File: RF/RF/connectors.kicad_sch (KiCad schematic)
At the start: 0 parts

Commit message: added external memory
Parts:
- added J601: Conn_01x02, Connector_PinHeader_2.00mm:PinHeader_1x02_P2.00mm_Vertical, symbol Connector_Generic:Conn_01x02
- added J602: Conn_01x06, Connector_PinHeader_2.00mm:PinHeader_1x06_P2.00mm_Vertical, symbol Connector_Generic:Conn_01x06
- added J603: Conn_02x05_Odd_Even, Connector_PinHeader_1.27mm:PinHeader_2x04_P1.27mm_Vertical_SMD, symbol Connector_Generic:Conn_02x05_Odd_Even
- added R601: DNP, Resistor_SMD:R_4020_10251Metric_Pad1.65x5.30mm_HandSolder, symbol Device:R
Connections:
- new net: J602.3 (Pin_3), R601.1
- new net +3.3V: J601.1 (Pin_1), J603.2 (Pin_2), R601.2
- new net +3.3VADC: J603.9 (Pin_9)
- new net CC_DC: J603.3 (Pin_3)
- new net CC_DD: J603.4 (Pin_4)
- new net CC_SPI_MISO: J603.10 (Pin_10)
- new net CC_SPI_MOSI: J603.8 (Pin_8)
- new net CC_SPI_SCK: J603.6 (Pin_6)
- new net GND: J601.2 (Pin_2), J602.1 (Pin_1), J603.1 (Pin_1)
- new net UART0_CTS: J602.6 (Pin_6)
- new net UART0_RTS: J602.2 (Pin_2)
- new net UART0_RX: J602.4 (Pin_4)
- new net UART0_TX: J602.5 (Pin_5)
- new net ~{CC_SPI_SSN}: J603.5 (Pin_5)
- new net ~{RESET}: J603.7 (Pin_7)
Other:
- note added: "(3V3 from debugger)"
- note added: "CC DEBUGGER"
- note added: "POWER INPUT"
- note added: "UART HEADER"

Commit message: RF: Push for schematic capture review version 1.0
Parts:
- J601: footprint Connector_PinHeader_2.00mm:PinHeader_1x02_P2.00mm_Vertical -> Connector_PinHeader_1.27mm:PinHeader_1x02_P1.27mm_Vertical
- J602: footprint Connector_PinHeader_2.00mm:PinHeader_1x06_P2.00mm_Vertical -> Connector_PinHeader_1.27mm:PinHeader_1x06_P1.27mm_Vertical
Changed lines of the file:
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@@
   )
   (rectangle (start 166.624 75.692) (end 229.362 104.648)
-    (stroke (width 0) (type default))
+    (stroke (width 0.5) (type default))
     (fill (type none))
   )
   (rectangle (start 52.324 73.66) (end 99.314 101.6)
-    (stroke (width 0) (type default))
+    (stroke (width 0.5) (type default))
     (fill (type none))
   )
   (rectangle (start 113.03 75.692) (end 148.59 99.06)
-    (stroke (width 0) (type default))
+    (stroke (width 0.5) (type default))
     (fill (type none))
   )
@@
       (effects (font (size 1.27 1.27)) (justify left))
     )
-    (property "Footprint" "Connector_PinHeader_2.00mm:PinHeader_1x02_P2.00mm_Vertical" (at 127.762 87.63 0)
+    (property "Footprint" "Connector_PinHeader_1.27mm:PinHeader_1x02_P1.27mm_Vertical" (at 127.762 87.63 0)
       (effects (font (size 1.27 1.27)) hide)
     )
@@
       (effects (font (size 1.27 1.27)) (justify left))
     )
-    (property "Footprint" "Connector_PinHeader_2.00mm:PinHeader_1x06_P2.00mm_Vertical" (at 67.31 90.678 0)
-      (effects (font (size 1.27 1.27)) hide)
-    )
+    (property "Footprint" "Connector_PinHeader_1.27mm:PinHeader_1x06_P1.27mm_Vertical" (at 67.31 90.678 0)
+      (effects (font (size 1.27 1.27)) hide)
+    )

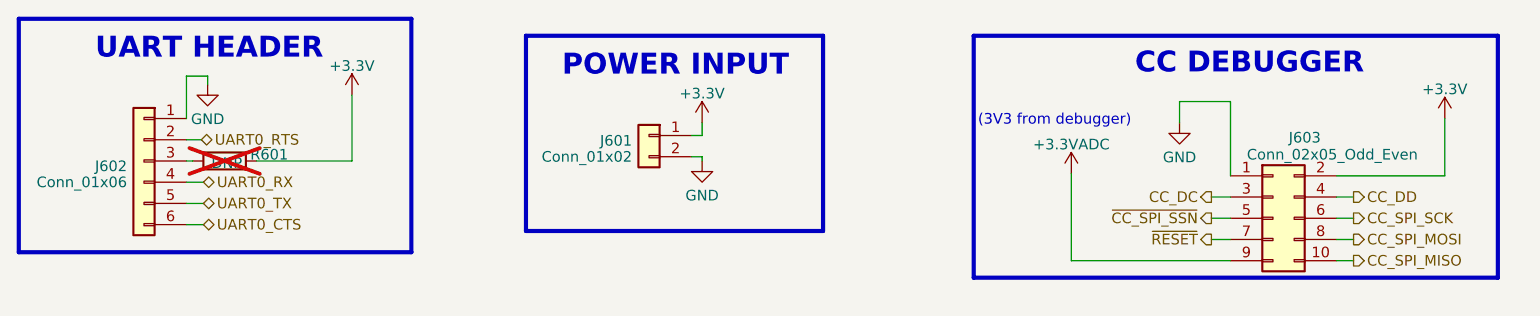
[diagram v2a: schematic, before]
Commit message: added standard connector and some initial layout
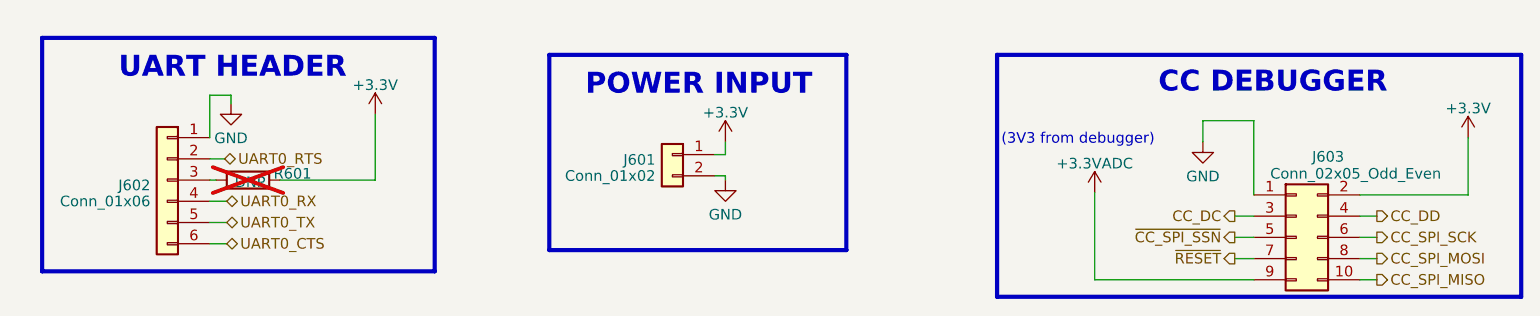
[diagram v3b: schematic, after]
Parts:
- R601: footprint Resistor_SMD:R_4020_10251Metric_Pad1.65x5.30mm_HandSolder -> Resistor_SMD:R_0603_1608Metric_Pad0.98x0.95mm_HandSolder
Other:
- moved on the sheet: J601, J602, J603, R601

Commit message: layout rev 1.0
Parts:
- J603: footprint Connector_PinHeader_1.27mm:PinHeader_2x04_P1.27mm_Vertical_SMD -> Connector_PinHeader_1.27mm:PinHeader_2x05_P1.27mm_Vertical_SMD
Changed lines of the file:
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@@
       (effects (font (size 1.27 1.27)))
     )
-    (property "Footprint" "Connector_PinHeader_1.27mm:PinHeader_2x04_P1.27mm_Vertical_SMD" (at 205.232 99.822 0)
+    (property "Footprint" "Connector_PinHeader_1.27mm:PinHeader_2x05_P1.27mm_Vertical_SMD" (at 205.232 99.822 0)
       (effects (font (size 1.27 1.27)) hide)
     )
